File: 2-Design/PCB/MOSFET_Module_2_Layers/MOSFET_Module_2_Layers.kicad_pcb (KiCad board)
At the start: 2 copper layers, 60 x 47 mm, 14 parts, among them J1 Conn_01x04_Male, J2 Conn_01x04_Male, Q1 SPW47N60, Q2 SPW47N60

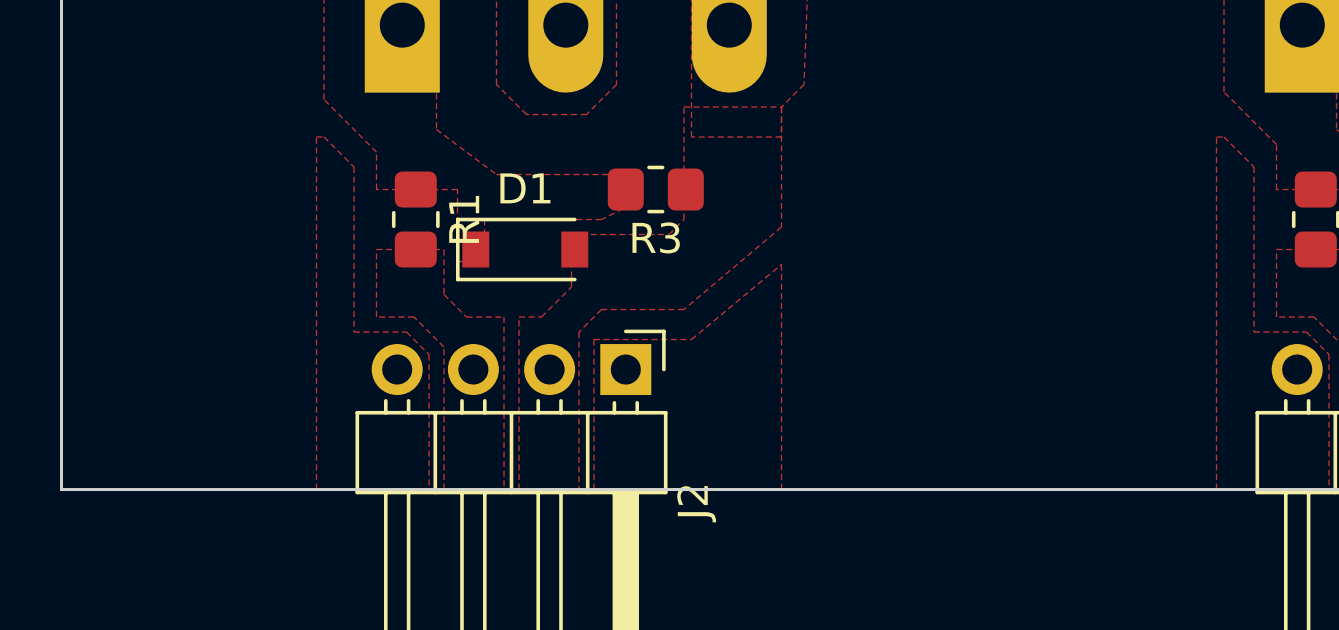
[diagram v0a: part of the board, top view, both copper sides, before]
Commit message: Controller Module v1, tracks to be drawn
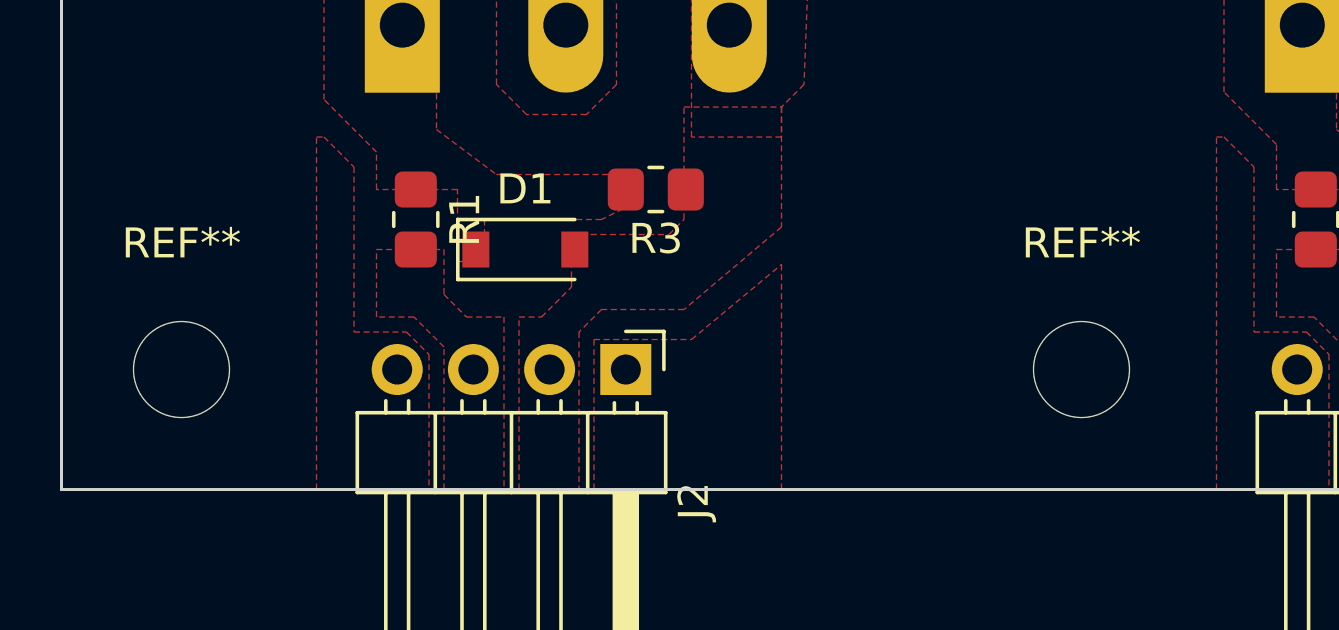
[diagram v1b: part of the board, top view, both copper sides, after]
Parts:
- added REF**: MountingHole_3.2mm_M3, MountingHole:MountingHole_3.2mm_M3, F.Cu at (84.0, 108.0)
- added REF**: MountingHole_3.2mm_M3, MountingHole:MountingHole_3.2mm_M3, F.Cu at (54.0, 108.0)
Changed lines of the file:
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@@
     )
+  )
+  (footprint "MountingHole:MountingHole_3.2mm_M3" (layer "F.Cu")
+    (at 84 108)
+    (descr "Mounting Hole 3.2mm, no annular, M3")
+    (tags "mounting hole 3.2mm no annular m3")
+    (attr exclude_from_pos_files exclude_from_bom)
+    (fp_text reference "REF**" (at 0 -4.2) (layer "F.SilkS")
+      (effects (font (size 1 1) (thickness 0.15)))
+    )
+    (fp_text value "MountingHole_3.2mm_M3" (at -4.6 0.4 90) (layer "F.Fab")
+      (effects (font (size 1 1) (thickness 0.15)))
+    )
+    (fp_text user "${REFERENCE}" (at 0.3 0) (layer "F.Fab")
+      (effects (font (size 1 1) (thickness 0.15)))
+    )
+    (fp_circle (center 0 0) (end 3.2 0) (layer "Cmts.User") (width 0.15) (fill none))
+    (fp_circle (center 0 0) (end 3.45 0) (layer "F.CrtYd") (width 0.05) (fill none))
+    (pad "" np_thru_hole circle (at 0 0) (size 3.2 3.2) (drill 3.2) (layers *.Cu *.Mask))
+  )
+  (footprint "MountingHole:MountingHole_3.2mm_M3" (layer "F.Cu")
+    (at 54 108)
+    (descr "Mounting Hole 3.2mm, no annular, M3")
+    (tags "mounting hole 3.2mm no annular m3")
+    (attr exclude_from_pos_files exclude_from_bom)
+    (fp_text reference "REF**" (at 0 -4.2) (layer "F.SilkS")
+      (effects (font (size 1 1) (thickness 0.15)))
+    )
+    (fp_text value "MountingHole_3.2mm_M3" (at -6.2 0.5 90) (layer "F.Fab")
+      (effects (font (size 1 1) (thickness 0.15)))
+    )
+    (fp_text user "${REFERENCE}" (at 0.3 0) (layer "F.Fab")
+      (effects (font (size 1 1) (thickness 0.15)))
+    )
+    (fp_circle (center 0 0) (end 3.2 0) (layer "Cmts.User") (width 0.15) (fill none))
+    (fp_circle (center 0 0) (end 3.45 0) (layer "F.CrtYd") (width 0.05) (fill none))
+    (pad "" np_thru_hole circle (at 0 0) (size 3.2 3.2) (drill 3.2) (layers *.Cu *.Mask))
   )
   (footprint "Capacitor_SMD:C_1210_3225Metric_Pad1.33x2.70mm_HandSolder" (layer "F.Cu")

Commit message: Some changes i dont even remember
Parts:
- removed the C1 at (61.4, 81.5)
- removed the C2 at (61.4, 89.3)
- removed the C3 at (61.4, 77.5)
- removed the C4 at (61.4, 85.3)
- removed the D1 at (65.5, 104.0)
- removed the D2 at (95.5, 104.0)
- removed the J1 at (98.8, 108.0)
- removed the J2 at (68.8, 108.0)
- removed the Q1 at (61.4, 96.5)
- removed the Q2 at (91.4, 96.5)
- removed the R1 at (61.8, 103.0)
- removed the R2 at (91.8, 103.0)
- removed the R3 at (69.8, 102.0)
- removed the R4 at (99.8, 102.0)
- removed the REF** at (84.0, 108.0)
- removed the REF** at (54.0, 108.0)
- added C1: 1uF, Capacitor_SMD:C_1210_3225Metric_Pad1.33x2.70mm_HandSolder, F.Cu at (-58.1, 29.0)
- added C1: 1uF, Capacitor_SMD:C_1210_3225Metric_Pad1.33x2.70mm_HandSolder, F.Cu at (167.9, -92.5)
- added C1: 1uF, Capacitor_SMD:C_1210_3225Metric_Pad1.33x2.70mm_HandSolder, F.Cu at (163.9, 65.5)
- added C1: 1uF, Capacitor_SMD:C_1210_3225Metric_Pad1.33x2.70mm_HandSolder, F.Cu at (167.7, -42.5)
- added C1: 1uF, Capacitor_SMD:C_1210_3225Metric_Pad1.33x2.70mm_HandSolder, F.Cu at (163.9, 116.5)
- added C1: 1uF, Capacitor_SMD:C_1210_3225Metric_Pad1.33x2.70mm_HandSolder, F.Cu at (99.9, 116.5)
- added C1: 1uF, Capacitor_SMD:C_1210_3225Metric_Pad1.33x2.70mm_HandSolder, F.Cu at (99.9, 65.5)
- added C1: 1uF, Capacitor_SMD:C_1210_3225Metric_Pad1.33x2.70mm_HandSolder, F.Cu at (103.9, -92.5)
- added C1: 1uF, Capacitor_SMD:C_1210_3225Metric_Pad1.33x2.70mm_HandSolder, F.Cu at (-67.6, 118.5)
- added C1: 1uF, Capacitor_SMD:C_1210_3225Metric_Pad1.33x2.70mm_HandSolder, F.Cu at (103.9, -42.5)
- added C2: 1uF, Capacitor_SMD:C_1210_3225Metric_Pad1.33x2.70mm_HandSolder, F.Cu at (163.9, 73.3)
- added C2: 1uF, Capacitor_SMD:C_1210_3225Metric_Pad1.33x2.70mm_HandSolder, F.Cu at (-67.6, 126.3)
- added C2: 1uF, Capacitor_SMD:C_1210_3225Metric_Pad1.33x2.70mm_HandSolder, F.Cu at (103.9, -34.7)
- added C2: 1uF, Capacitor_SMD:C_1210_3225Metric_Pad1.33x2.70mm_HandSolder, F.Cu at (167.9, -84.7)
- added C2: 1uF, Capacitor_SMD:C_1210_3225Metric_Pad1.33x2.70mm_HandSolder, F.Cu at (99.9, 73.3)
- added C2: 1uF, Capacitor_SMD:C_1210_3225Metric_Pad1.33x2.70mm_HandSolder, F.Cu at (163.9, 124.3)
- added C2: 1uF, Capacitor_SMD:C_1210_3225Metric_Pad1.33x2.70mm_HandSolder, F.Cu at (-58.1, 36.8)
- added C2: 1uF, Capacitor_SMD:C_1210_3225Metric_Pad1.33x2.70mm_HandSolder, F.Cu at (167.7, -34.7)
- added C2: 1uF, Capacitor_SMD:C_1210_3225Metric_Pad1.33x2.70mm_HandSolder, F.Cu at (103.9, -84.7)
- added C2: 1uF, Capacitor_SMD:C_1210_3225Metric_Pad1.33x2.70mm_HandSolder, F.Cu at (99.9, 124.3)
- added C3: 1uF, Capacitor_SMD:C_1210_3225Metric_Pad1.33x2.70mm_HandSolder, F.Cu at (103.9, -96.5)
- added C3: 1uF, Capacitor_SMD:C_1210_3225Metric_Pad1.33x2.70mm_HandSolder, F.Cu at (163.9, 61.5)
- added C3: 1uF, Capacitor_SMD:C_1210_3225Metric_Pad1.33x2.70mm_HandSolder, F.Cu at (103.9, -46.5)
- added C3: 1uF, Capacitor_SMD:C_1210_3225Metric_Pad1.33x2.70mm_HandSolder, F.Cu at (163.9, 112.5)
- added C3: 1uF, Capacitor_SMD:C_1210_3225Metric_Pad1.33x2.70mm_HandSolder, F.Cu at (-58.1, 25.0)
- added C3: 1uF, Capacitor_SMD:C_1210_3225Metric_Pad1.33x2.70mm_HandSolder, F.Cu at (-67.6, 114.5)
- added C3: 1uF, Capacitor_SMD:C_1210_3225Metric_Pad1.33x2.70mm_HandSolder, F.Cu at (99.9, 112.5)
- added C3: 1uF, Capacitor_SMD:C_1210_3225Metric_Pad1.33x2.70mm_HandSolder, F.Cu at (167.7, -46.5)
- added C3: 1uF, Capacitor_SMD:C_1210_3225Metric_Pad1.33x2.70mm_HandSolder, F.Cu at (167.9, -96.5)
- added C3: 1uF, Capacitor_SMD:C_1210_3225Metric_Pad1.33x2.70mm_HandSolder, F.Cu at (99.9, 61.5)
- added C4: 1uF, Capacitor_SMD:C_1210_3225Metric_Pad1.33x2.70mm_HandSolder, F.Cu at (103.9, -88.7)
- added C4: 1uF, Capacitor_SMD:C_1210_3225Metric_Pad1.33x2.70mm_HandSolder, F.Cu at (-67.6, 122.3)
- added C4: 1uF, Capacitor_SMD:C_1210_3225Metric_Pad1.33x2.70mm_HandSolder, F.Cu at (99.9, 120.3)
- added C4: 1uF, Capacitor_SMD:C_1210_3225Metric_Pad1.33x2.70mm_HandSolder, F.Cu at (99.9, 69.3)
- added C4: 1uF, Capacitor_SMD:C_1210_3225Metric_Pad1.33x2.70mm_HandSolder, F.Cu at (-58.1, 32.8)
- added C4: 1uF, Capacitor_SMD:C_1210_3225Metric_Pad1.33x2.70mm_HandSolder, F.Cu at (163.9, 120.3)
- added C4: 1uF, Capacitor_SMD:C_1210_3225Metric_Pad1.33x2.70mm_HandSolder, F.Cu at (167.9, -88.7)
- added C4: 1uF, Capacitor_SMD:C_1210_3225Metric_Pad1.33x2.70mm_HandSolder, F.Cu at (103.9, -38.7)
- added C4: 1uF, Capacitor_SMD:C_1210_3225Metric_Pad1.33x2.70mm_HandSolder, F.Cu at (167.7, -38.7)
- added C4: 1uF, Capacitor_SMD:C_1210_3225Metric_Pad1.33x2.70mm_HandSolder, F.Cu at (163.9, 69.3)
- added D1: D_Zener, Diode_SMD:D_SOD-123, F.Cu at (168.0, 139.0)
- added D1: D_Zener, Diode_SMD:D_SOD-123, F.Cu at (168.0, 88.0)
- added D1: D_Zener, Diode_SMD:D_SOD-123, F.Cu at (108.0, -70.0)
- added D1: D_Zener, Diode_SMD:D_SOD-123, F.Cu at (-54.0, 51.5)
- added D1: D_Zener, Diode_SMD:D_SOD-123, F.Cu at (104.0, 139.0)
- added D1: D_Zener, Diode_SMD:D_SOD-123, F.Cu at (171.7, -20.0)
- added D1: D_Zener, Diode_SMD:D_SOD-123, F.Cu at (108.0, -20.0)
- added D1: D_Zener, Diode_SMD:D_SOD-123, F.Cu at (104.0, 88.0)
- added D1: D_Zener, Diode_SMD:D_SOD-123, F.Cu at (-63.5, 141.0)
- added D1: D_Zener, Diode_SMD:D_SOD-123, F.Cu at (172.0, -70.0)
- added D2: D_Zener, Diode_SMD:D_SOD-123, F.Cu at (-33.5, 141.0)
- added D2: D_Zener, Diode_SMD:D_SOD-123, F.Cu at (134.0, 139.0)
- added D2: D_Zener, Diode_SMD:D_SOD-123, F.Cu at (134.0, 88.0)
- added D2: D_Zener, Diode_SMD:D_SOD-123, F.Cu at (201.7, -20.0)
- added D2: D_Zener, Diode_SMD:D_SOD-123, F.Cu at (198.0, 139.0)
- added D2: D_Zener, Diode_SMD:D_SOD-123, F.Cu at (138.0, -20.0)
- added D2: D_Zener, Diode_SMD:D_SOD-123, F.Cu at (-24.0, 51.5)
- added D2: D_Zener, Diode_SMD:D_SOD-123, F.Cu at (202.0, -70.0)
- added D2: D_Zener, Diode_SMD:D_SOD-123, F.Cu at (198.0, 88.0)
- added D2: D_Zener, Diode_SMD:D_SOD-123, F.Cu at (138.0, -70.0)
- added J1: Conn_01x04_Male, Connector_PinHeader_2.54mm:PinHeader_1x04_P2.54mm_Horizontal, F.Cu at (205.3, -66.0)
- added J1: Conn_01x04_Male, Connector_PinHeader_2.54mm:PinHeader_1x04_P2.54mm_Horizontal, F.Cu at (201.3, 143.0)
- added J1: Conn_01x04_Male, Connector_PinHeader_2.54mm:PinHeader_1x04_P2.54mm_Horizontal, F.Cu at (137.3, 92.0)
- added J1: Conn_01x04_Male, Connector_PinHeader_2.54mm:PinHeader_1x04_P2.54mm_Horizontal, F.Cu at (-20.7, 55.5)
- added J1: Conn_01x04_Male, Connector_PinHeader_2.54mm:PinHeader_1x04_P2.54mm_Horizontal, F.Cu at (141.3, -16.0)
- added J1: Conn_01x04_Male, Connector_PinHeader_2.54mm:PinHeader_1x04_P2.54mm_Horizontal, F.Cu at (201.3, 92.0)
- added J1: Conn_01x04_Male, Connector_PinHeader_2.54mm:PinHeader_1x04_P2.54mm_Horizontal, F.Cu at (137.3, 143.0)
- added J1: Conn_01x04_Male, Connector_PinHeader_2.54mm:PinHeader_1x04_P2.54mm_Horizontal, F.Cu at (141.3, -66.0)
- added J1: Conn_01x04_Male, Connector_PinHeader_2.54mm:PinHeader_1x04_P2.54mm_Horizontal, F.Cu at (205.1, -16.0)
- added J1: Conn_01x04_Male, Connector_PinHeader_2.54mm:PinHeader_1x04_P2.54mm_Horizontal, F.Cu at (-30.2, 145.0)
- added J2: Conn_01x04_Male, Connector_PinHeader_2.54mm:PinHeader_1x04_P2.54mm_Horizontal, F.Cu at (-50.7, 55.5)
- added J2: Conn_01x04_Male, Connector_PinHeader_2.54mm:PinHeader_1x04_P2.54mm_Horizontal, F.Cu at (-60.2, 145.0)
- added J2: Conn_01x04_Male, Connector_PinHeader_2.54mm:PinHeader_1x04_P2.54mm_Horizontal, F.Cu at (171.3, 92.0)
- added J2: Conn_01x04_Male, Connector_PinHeader_2.54mm:PinHeader_1x04_P2.54mm_Horizontal, F.Cu at (171.3, 143.0)
- added J2: Conn_01x04_Male, Connector_PinHeader_2.54mm:PinHeader_1x04_P2.54mm_Horizontal, F.Cu at (111.3, -66.0)
- added J2: Conn_01x04_Male, Connector_PinHeader_2.54mm:PinHeader_1x04_P2.54mm_Horizontal, F.Cu at (111.3, -16.0)
- added J2: Conn_01x04_Male, Connector_PinHeader_2.54mm:PinHeader_1x04_P2.54mm_Horizontal, F.Cu at (175.3, -66.0)
- added J2: Conn_01x04_Male, Connector_PinHeader_2.54mm:PinHeader_1x04_P2.54mm_Horizontal, F.Cu at (107.3, 92.0)
- added J2: Conn_01x04_Male, Connector_PinHeader_2.54mm:PinHeader_1x04_P2.54mm_Horizontal, F.Cu at (107.3, 143.0)
- added J2: Conn_01x04_Male, Connector_PinHeader_2.54mm:PinHeader_1x04_P2.54mm_Horizontal, F.Cu at (175.1, -16.0)
- added Q1: SPW47N60, ee463_footprint_lib:TO-247-3_Horizontal_TabDown_ee463, F.Cu at (163.9, 80.5)
- added Q1: SPW47N60, ee463_footprint_lib:TO-247-3_Horizontal_TabDown_ee463, F.Cu at (167.6, -27.5)
- added Q1: SPW47N60, ee463_footprint_lib:TO-247-3_Horizontal_TabDown_ee463, F.Cu at (163.9, 131.5)
- added Q1: SPW47N60, ee463_footprint_lib:TO-247-3_Horizontal_TabDown_ee463, F.Cu at (103.9, -77.5)
- added Q1: SPW47N60, ee463_footprint_lib:TO-247-3_Horizontal_TabDown_ee463, F.Cu at (167.9, -77.5)
- added Q1: SPW47N60, ee463_footprint_lib:TO-247-3_Horizontal_TabDown_ee463, F.Cu at (103.9, -27.5)
- added Q1: SPW47N60, ee463_footprint_lib:TO-247-3_Horizontal_TabDown_ee463, F.Cu at (-58.1, 44.0)
- added Q1: SPW47N60, ee463_footprint_lib:TO-247-3_Horizontal_TabDown_ee463, F.Cu at (99.9, 131.5)
- added Q1: SPW47N60, ee463_footprint_lib:TO-247-3_Horizontal_TabDown_ee463, F.Cu at (-67.6, 133.5)
- added Q1: SPW47N60, ee463_footprint_lib:TO-247-3_Horizontal_TabDown_ee463, F.Cu at (99.9, 80.5)
- added Q2: SPW47N60, ee463_footprint_lib:TO-247-3_Horizontal_TabDown_ee463, F.Cu at (193.9, 131.5)
- added Q2: SPW47N60, ee463_footprint_lib:TO-247-3_Horizontal_TabDown_ee463, F.Cu at (197.9, -77.5)
- added Q2: SPW47N60, ee463_footprint_lib:TO-247-3_Horizontal_TabDown_ee463, F.Cu at (-37.6, 133.5)
- added Q2: SPW47N60, ee463_footprint_lib:TO-247-3_Horizontal_TabDown_ee463, F.Cu at (129.9, 80.5)
- added Q2: SPW47N60, ee463_footprint_lib:TO-247-3_Horizontal_TabDown_ee463, F.Cu at (133.9, -27.5)
- added Q2: SPW47N60, ee463_footprint_lib:TO-247-3_Horizontal_TabDown_ee463, F.Cu at (129.9, 131.5)
- added Q2: SPW47N60, ee463_footprint_lib:TO-247-3_Horizontal_TabDown_ee463, F.Cu at (133.9, -77.5)
- added Q2: SPW47N60, ee463_footprint_lib:TO-247-3_Horizontal_TabDown_ee463, F.Cu at (-28.1, 44.0)
- added Q2: SPW47N60, ee463_footprint_lib:TO-247-3_Horizontal_TabDown_ee463, F.Cu at (197.6, -27.5)
- added Q2: SPW47N60, ee463_footprint_lib:TO-247-3_Horizontal_TabDown_ee463, F.Cu at (193.9, 80.5)
- added R1: ??, Resistor_SMD:R_0805_2012Metric_Pad1.20x1.40mm_HandSolder, F.Cu at (164.3, 138.0)
- added R1: ??, Resistor_SMD:R_0805_2012Metric_Pad1.20x1.40mm_HandSolder, F.Cu at (100.3, 87.0)
- added R1: ??, Resistor_SMD:R_0805_2012Metric_Pad1.20x1.40mm_HandSolder, F.Cu at (104.3, -71.0)
- added R1: ??, Resistor_SMD:R_0805_2012Metric_Pad1.20x1.40mm_HandSolder, F.Cu at (-57.7, 50.5)
- added R1: ??, Resistor_SMD:R_0805_2012Metric_Pad1.20x1.40mm_HandSolder, F.Cu at (168.3, -71.0)
- added R1: ??, Resistor_SMD:R_0805_2012Metric_Pad1.20x1.40mm_HandSolder, F.Cu at (164.3, 87.0)
- added R1: ??, Resistor_SMD:R_0805_2012Metric_Pad1.20x1.40mm_HandSolder, F.Cu at (104.3, -21.0)
- added R1: ??, Resistor_SMD:R_0805_2012Metric_Pad1.20x1.40mm_HandSolder, F.Cu at (168.1, -21.0)
- added R1: ??, Resistor_SMD:R_0805_2012Metric_Pad1.20x1.40mm_HandSolder, F.Cu at (100.3, 138.0)
- added R1: ??, Resistor_SMD:R_0805_2012Metric_Pad1.20x1.40mm_HandSolder, F.Cu at (-67.2, 140.0)
- added R2: ??, Resistor_SMD:R_0805_2012Metric_Pad1.20x1.40mm_HandSolder, F.Cu at (-27.7, 50.5)
- added R2: ??, Resistor_SMD:R_0805_2012Metric_Pad1.20x1.40mm_HandSolder, F.Cu at (194.3, 138.0)
- added R2: ??, Resistor_SMD:R_0805_2012Metric_Pad1.20x1.40mm_HandSolder, F.Cu at (198.3, -71.0)
- added R2: ??, Resistor_SMD:R_0805_2012Metric_Pad1.20x1.40mm_HandSolder, F.Cu at (130.3, 138.0)
- added R2: ??, Resistor_SMD:R_0805_2012Metric_Pad1.20x1.40mm_HandSolder, F.Cu at (134.3, -71.0)
- added R2: ??, Resistor_SMD:R_0805_2012Metric_Pad1.20x1.40mm_HandSolder, F.Cu at (134.3, -21.0)
- added R2: ??, Resistor_SMD:R_0805_2012Metric_Pad1.20x1.40mm_HandSolder, F.Cu at (194.3, 87.0)
- added R2: ??, Resistor_SMD:R_0805_2012Metric_Pad1.20x1.40mm_HandSolder, F.Cu at (-37.2, 140.0)
- added R2: ??, Resistor_SMD:R_0805_2012Metric_Pad1.20x1.40mm_HandSolder, F.Cu at (130.3, 87.0)
- added R2: ??, Resistor_SMD:R_0805_2012Metric_Pad1.20x1.40mm_HandSolder, F.Cu at (198.1, -21.0)
- added R3: 10kR, Resistor_SMD:R_0805_2012Metric_Pad1.20x1.40mm_HandSolder, F.Cu at (112.3, -72.0)
- added R3: 10kR, Resistor_SMD:R_0805_2012Metric_Pad1.20x1.40mm_HandSolder, F.Cu at (112.3, -22.0)
- added R3: 10kR, Resistor_SMD:R_0805_2012Metric_Pad1.20x1.40mm_HandSolder, F.Cu at (-59.2, 139.0)
- added R3: 10kR, Resistor_SMD:R_0805_2012Metric_Pad1.20x1.40mm_HandSolder, F.Cu at (176.1, -22.0)
- added R3: 10kR, Resistor_SMD:R_0805_2012Metric_Pad1.20x1.40mm_HandSolder, F.Cu at (176.3, -72.0)
- added R3: 10kR, Resistor_SMD:R_0805_2012Metric_Pad1.20x1.40mm_HandSolder, F.Cu at (172.3, 137.0)
- added R3: 10kR, Resistor_SMD:R_0805_2012Metric_Pad1.20x1.40mm_HandSolder, F.Cu at (-49.7, 49.5)
- added R3: 10kR, Resistor_SMD:R_0805_2012Metric_Pad1.20x1.40mm_HandSolder, F.Cu at (108.3, 86.0)
- added R3: 10kR, Resistor_SMD:R_0805_2012Metric_Pad1.20x1.40mm_HandSolder, F.Cu at (108.3, 137.0)
- added R3: 10kR, Resistor_SMD:R_0805_2012Metric_Pad1.20x1.40mm_HandSolder, F.Cu at (172.3, 86.0)
- added R4: 10kR, Resistor_SMD:R_0805_2012Metric_Pad1.20x1.40mm_HandSolder, F.Cu at (142.3, -72.0)
- added R4: 10kR, Resistor_SMD:R_0805_2012Metric_Pad1.20x1.40mm_HandSolder, F.Cu at (-19.7, 49.5)
- added R4: 10kR, Resistor_SMD:R_0805_2012Metric_Pad1.20x1.40mm_HandSolder, F.Cu at (138.3, 86.0)
- added R4: 10kR, Resistor_SMD:R_0805_2012Metric_Pad1.20x1.40mm_HandSolder, F.Cu at (-29.2, 139.0)
- added R4: 10kR, Resistor_SMD:R_0805_2012Metric_Pad1.20x1.40mm_HandSolder, F.Cu at (206.3, -72.0)
- added R4: 10kR, Resistor_SMD:R_0805_2012Metric_Pad1.20x1.40mm_HandSolder, F.Cu at (202.3, 137.0)
- added R4: 10kR, Resistor_SMD:R_0805_2012Metric_Pad1.20x1.40mm_HandSolder, F.Cu at (138.3, 137.0)
- added R4: 10kR, Resistor_SMD:R_0805_2012Metric_Pad1.20x1.40mm_HandSolder, F.Cu at (202.3, 86.0)
- added R4: 10kR, Resistor_SMD:R_0805_2012Metric_Pad1.20x1.40mm_HandSolder, F.Cu at (206.1, -22.0)
- added R4: 10kR, Resistor_SMD:R_0805_2012Metric_Pad1.20x1.40mm_HandSolder, F.Cu at (142.3, -22.0)
- added REF**: MountingHole_3.2mm_M3, MountingHole:MountingHole_3.2mm_M3, F.Cu at (160.2, -16.0)
- added REF**: MountingHole_3.2mm_M3, MountingHole:MountingHole_3.2mm_M3, F.Cu at (122.5, 143.0)
- added REF**: MountingHole_3.2mm_M3, MountingHole:MountingHole_3.2mm_M3, F.Cu at (-45.0, 145.0)
- added REF**: MountingHole_3.2mm_M3, MountingHole:MountingHole_3.2mm_M3, F.Cu at (-75.0, 145.0)
- added REF**: MountingHole_3.2mm_M3, MountingHole:MountingHole_3.2mm_M3, F.Cu at (186.5, 143.0)
- added REF**: MountingHole_3.2mm_M3, MountingHole:MountingHole_3.2mm_M3, F.Cu at (190.2, -16.0)
- added REF**: MountingHole_3.2mm_M3, MountingHole:MountingHole_3.2mm_M3, F.Cu at (126.5, -16.0)
- added REF**: MountingHole_3.2mm_M3, MountingHole:MountingHole_3.2mm_M3, F.Cu at (92.5, 143.0)
- added REF**: MountingHole_3.2mm_M3, MountingHole:MountingHole_3.2mm_M3, F.Cu at (190.5, -66.0)
- added REF**: MountingHole_3.2mm_M3, MountingHole:MountingHole_3.2mm_M3, F.Cu at (156.5, 92.0)
- added REF**: MountingHole_3.2mm_M3, MountingHole:MountingHole_3.2mm_M3, F.Cu at (156.5, 143.0)
- added REF**: MountingHole_3.2mm_M3, MountingHole:MountingHole_3.2mm_M3, F.Cu at (126.5, -66.0)
- added REF**: MountingHole_3.2mm_M3, MountingHole:MountingHole_3.2mm_M3, F.Cu at (96.5, -66.0)
- added REF**: MountingHole_3.2mm_M3, MountingHole:MountingHole_3.2mm_M3, F.Cu at (122.5, 92.0)
- added REF**: MountingHole_3.2mm_M3, MountingHole:MountingHole_3.2mm_M3, F.Cu at (-35.5, 55.5)
- added REF**: MountingHole_3.2mm_M3, MountingHole:MountingHole_3.2mm_M3, F.Cu at (186.5, 92.0)
- added REF**: MountingHole_3.2mm_M3, MountingHole:MountingHole_3.2mm_M3, F.Cu at (92.5, 92.0)
- added REF**: MountingHole_3.2mm_M3, MountingHole:MountingHole_3.2mm_M3, F.Cu at (160.5, -66.0)
- added REF**: MountingHole_3.2mm_M3, MountingHole:MountingHole_3.2mm_M3, F.Cu at (-65.5, 55.5)
- added REF**: MountingHole_3.2mm_M3, MountingHole:MountingHole_3.2mm_M3, F.Cu at (96.5, -16.0)
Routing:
- net Net-(D1-Pad1): track 0.64 -> 6.36 mm
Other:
- board size 60 x 47 mm -> 297.5 x 260 mm
